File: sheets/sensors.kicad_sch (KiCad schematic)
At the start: 14 parts, among them CN1 StemmaQT, U6 SparkfunM9N, U7 BMP581, U8 ADXL345BCCZ-RL7, U9 ADXL375BCCZ-RL7

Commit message: some footprints assigned
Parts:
- CIO2, CS1: value 0.1u -> 100n
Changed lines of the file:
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@@
 			)
 		)
-		(property "Value" "0.1u"
+		(property "Value" "100n"
 			(at 227.33 29.2099 0)
 			(effects
@@
 			)
 		)
-		(property "Value" "0.1u"
+		(property "Value" "100n"
 			(at 172.466 113.03 0)
 			(effects

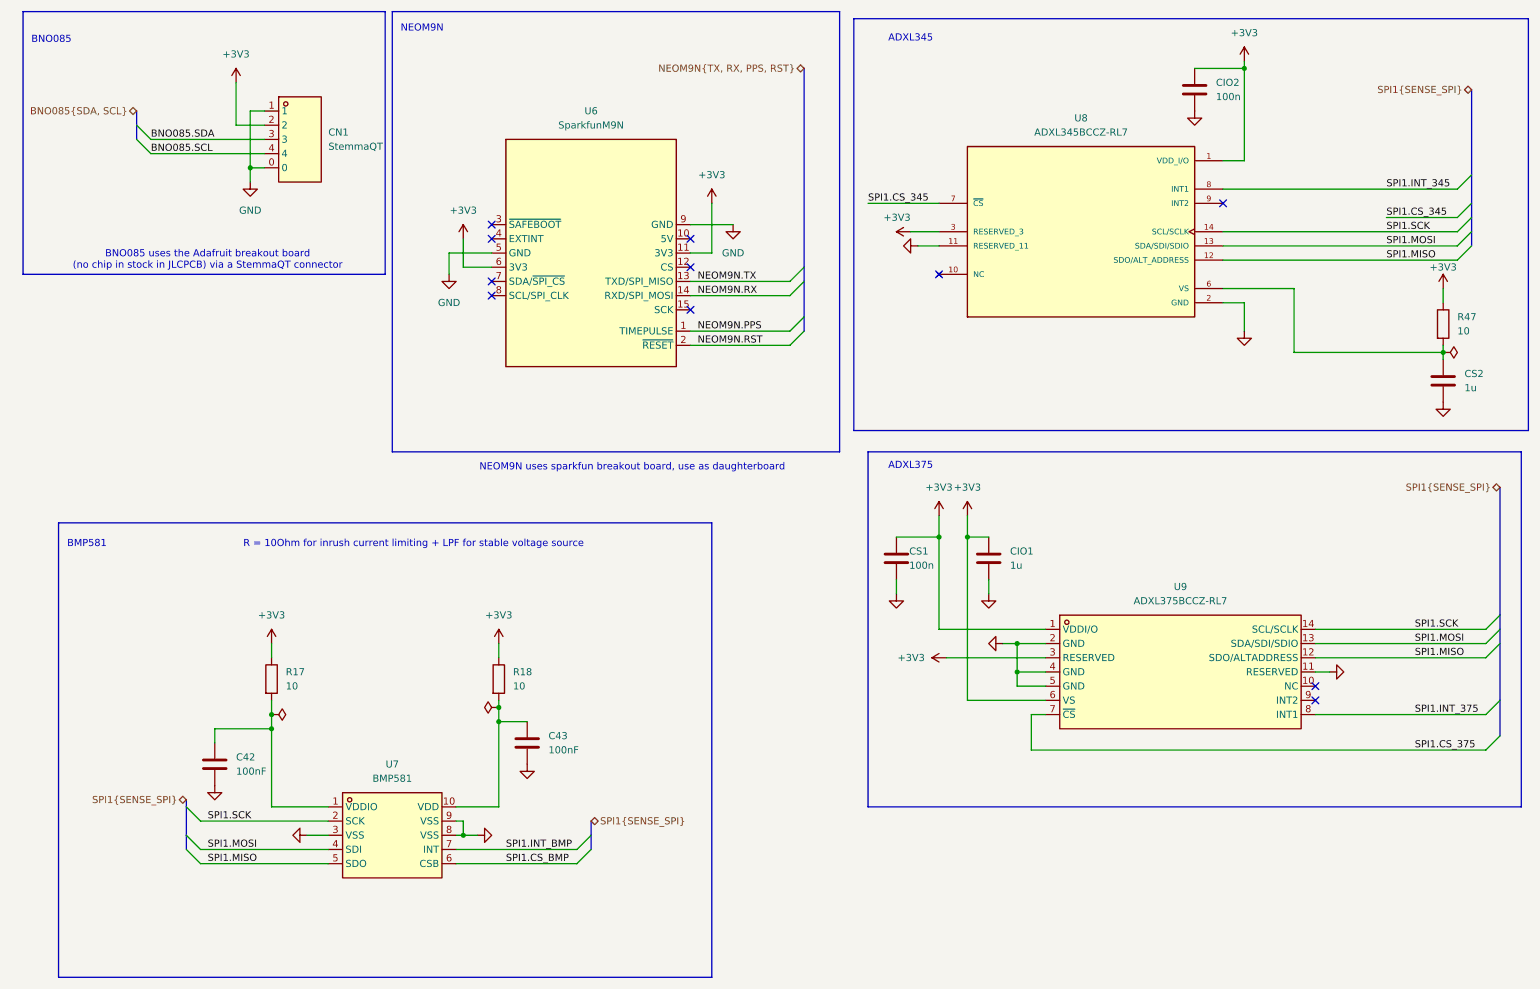
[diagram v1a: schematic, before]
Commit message: letter size schematic pages formatted
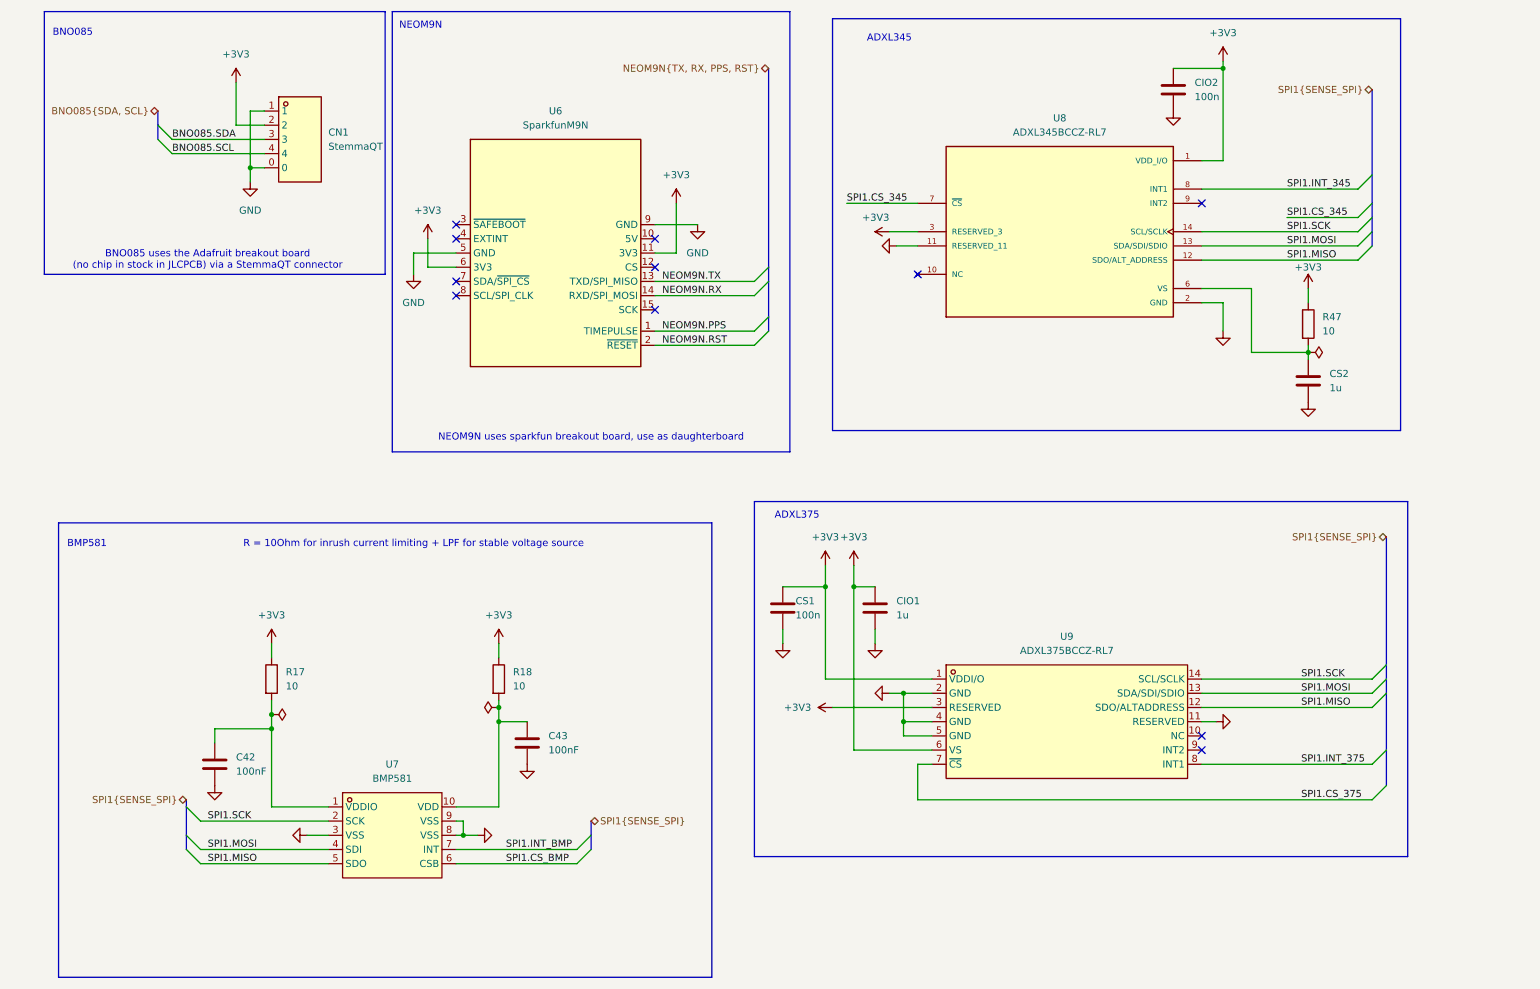
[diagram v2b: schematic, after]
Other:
- moved on the sheet: CIO1, CIO2, CS1, CS2, R47, U6, U8, U9
